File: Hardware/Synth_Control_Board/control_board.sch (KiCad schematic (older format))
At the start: 90 parts, among them J1 Conn_02x13_Odd_Even, J10 Conn_01x05, J11 Conn_01x08, J2 Conn_01x03, J3 Conn_02x13_Odd_Even, J4 Conn_01x08, J7 Conn_01x05, J8 Conn_01x05, J9 Conn_01x05, SW1 SW_DPDT_x2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

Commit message: fix net naming error on control board
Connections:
- net delay_in_1 is gone; now on net delay_fb_in: RV26.1
- net delay_in_2 is gone; now on net delay_time_in: RV27.1
- net delay_out_1 is gone; now on net delay_fb_out: RV26.2
- net delay_out_2 is gone; now on net delay_time_out: RV27.2
- net delay_out_3 is gone; now on net delay_mix_out: RV28.3
- net delay_in: no longer J4.5 (Pin_5)
- net delay_in_3 renamed delay_mix_in
- net delay_mix_in: now also J4.5 (Pin_5)
- net delay_out renamed delay_mix_out
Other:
- note added: "Global FB knob"
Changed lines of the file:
@@
 Delay controls
 Text Label 5600 4650 0    60   ~ 0
-delay_in_1
+delay_fb_in
 Text Label 5600 4750 0    60   ~ 0
-delay_out_1
+delay_fb_out
 Text Label 5600 4850 0    60   ~ 0
-delay_in_2
+delay_time_in
 Text Label 5600 4950 0    60   ~ 0
-delay_out_2
+delay_time_out
 Text Label 5600 5050 0    60   ~ 0
-delay_in_3
+delay_mix_in
 Text Label 5600 5150 0    60   ~ 0
-delay_out_3
+delay_mix_out
 Text Label 5350 6950 2    60   ~ 0
 delay_fb_in
@@
 delay_time_out
 Text Label 5350 7350 2    60   ~ 0
-delay_in
+delay_mix_in
 Text Label 5350 7450 2    60   ~ 0
-delay_out
+delay_mix_out
 $Comp
 L Conn_02x13_Odd_Even J1
@@
 	1    0    0    -1
 $EndComp
+Text Notes 3650 7900 0    60   ~ 0
+Global FB knob
 $EndSCHEMATC

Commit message: fix backward filter potentiometers
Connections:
- net freq_fb_1: now also RV17.A2 (S); no longer RV17.B2 (S)
- net freq_fb_2: now also RV14.A2 (S); no longer RV14.B2 (S)
- net freq_fb_3: now also RV15.A2 (S); no longer RV15.B2 (S)
- net freq_fb_4: now also RV16.A2 (S); no longer RV16.B2 (S)
- net freq_in_1: no longer RV17.A2 (S)
- net freq_in_2: no longer RV14.A2 (S)
- net freq_in_3: no longer RV15.A2 (S)
- net freq_in_4: no longer RV16.A2 (S)
- net freq_out_1: now also RV17.B2 (S)
- net freq_out_2: now also RV14.B2 (S)
- net freq_out_3: now also RV15.B2 (S)
- net freq_out_4: now also RV16.B2 (S)
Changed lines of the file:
@@
 Text Label 1800 6000 2    60   ~ 0
 freq_fb_1
-Text Label 1800 6600 2    60   ~ 0
+Text Label 1800 6550 2    60   ~ 0
 freq_fb_2
 Text Label 1800 7050 2    60   ~ 0
@@
 	1800 6300 2000 6300
 Wire Wire Line
-	1950 6050 2300 6050
-Connection ~ 1150 6300
-Wire Wire Line
 	1000 6300 1200 6300
 Wire Wire Line
-	1150 6050 1150 6300
-Wire Wire Line
-	1150 6050 1500 6050
-Wire Wire Line
 	8900 1700 9150 1700
 Wire Wire Line
@@
 	1400 6650 1400 6600
 Wire Wire Line
-	1400 6600 1050 6600
-Wire Wire Line
-	1050 6600 1050 6850
-Connection ~ 1050 6850
-Wire Wire Line
-	1800 6600 1800 6850
+	1800 6550 1800 6850
 Connection ~ 1800 6850
 Wire Wire Line
 	2250 6650 2250 6600
 Wire Wire Line
-	2250 6600 1900 6600
-Wire Wire Line
-	1900 6600 1900 6850
-Connection ~ 1900 6850
-Wire Wire Line
 	950  7350 1100 7350
 Wire Wire Line
 	1400 7150 1400 7100
-Wire Wire Line
-	1400 7100 1050 7100
-Wire Wire Line
-	1050 7100 1050 7350
-Connection ~ 1050 7350
 Wire Wire Line
 	1700 7350 1950 7350
@@
 	2250 7150 2250 7100
 Wire Wire Line
-	2250 7100 1900 7100
-Wire Wire Line
-	1900 7100 1900 7350
-Connection ~ 1900 7350
-Wire Wire Line
 	2550 7350 2750 7350
 Wire Wire Line
@@
 Wire Wire Line
 	1400 7600 1400 7550
-Wire Wire Line
-	1400 7550 1050 7550
-Wire Wire Line
-	1050 7550 1050 7800
-Connection ~ 1050 7800
 Wire Wire Line
 	1700 7800 1950 7800
@@
 	2250 7600 2250 7550
 Wire Wire Line
-	2250 7550 1900 7550
-Wire Wire Line
-	1900 7550 1900 7800
-Connection ~ 1900 7800
-Wire Wire Line
 	2550 7800 2750 7800
-Wire Wire Line
-	1950 6050 1950 6300
-Connection ~ 1950 6300
 $Comp
 L POT_DUAL RV17
@@
 Text Notes 3650 7900 0    60   ~ 0
 Global FB knob
+Wire Wire Line
+	1500 6050 1800 6050
+Connection ~ 1800 6050
+Wire Wire Line
+	2300 6050 2650 6050
+Wire Wire Line
+	2650 6050 2650 6300
+Connection ~ 2650 6300
+Wire Wire Line
+	2250 6600 2650 6600
+Wire Wire Line
+	2650 6600 2650 6850
+Connection ~ 2650 6850
+Wire Wire Line
+	2250 7100 2650 7100
+Wire Wire Line
+	2650 7100 2650 7350
+Connection ~ 2650 7350
+Wire Wire Line
+	2250 7550 2650 7550
+Wire Wire Line
+	2650 7550 2650 7800
+Connection ~ 2650 7800
+Wire Wire Line
+	1400 7550 1800 7550
+Connection ~ 1800 7550
+Wire Wire Line
+	1400 7100 1800 7100
+Connection ~ 1800 7100
+Wire Wire Line
+	1400 6600 1800 6600
+Connection ~ 1800 6600
 $EndSCHEMATC

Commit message: increase delay time pot value. End stop resistor is still fine.
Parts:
- RV27: value 20kA -> 100kA
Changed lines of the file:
@@
 P 4650 4700
 F 0 "RV27" V 4475 4700 50  0000 C CNN
-F 1 "20kA" V 4550 4700 50  0000 C CNN
+F 1 "100kA" V 4550 4700 50  0000 C CNN
 F 2 "Potentiometers:Potentiometer_Bourns_PTV09A-1_Horizontal" H 4650 4700 50  0001 C CNN
 F 3 "" H 4650 4700 50  0001 C CNN

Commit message: change delay fb control to log taper.
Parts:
- RV26: value 50kA -> 50kB
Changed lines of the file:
@@
 P 4650 4050
 F 0 "RV26" V 4475 4050 50  0000 C CNN
-F 1 "50kA" V 4550 4050 50  0000 C CNN
+F 1 "50kB" V 4550 4050 50  0000 C CNN
 F 2 "Potentiometers:Potentiometer_Bourns_PTV09A-1_Horizontal" H 4650 4050 50  0001 C CNN
 F 3 "" H 4650 4050 50  0001 C CNN

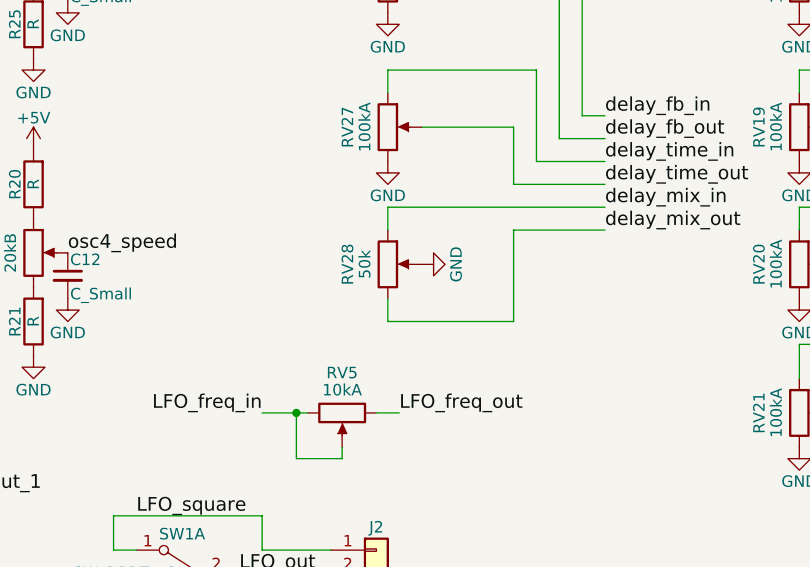
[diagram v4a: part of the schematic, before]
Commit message: WIP, delay mix control -> dual pot
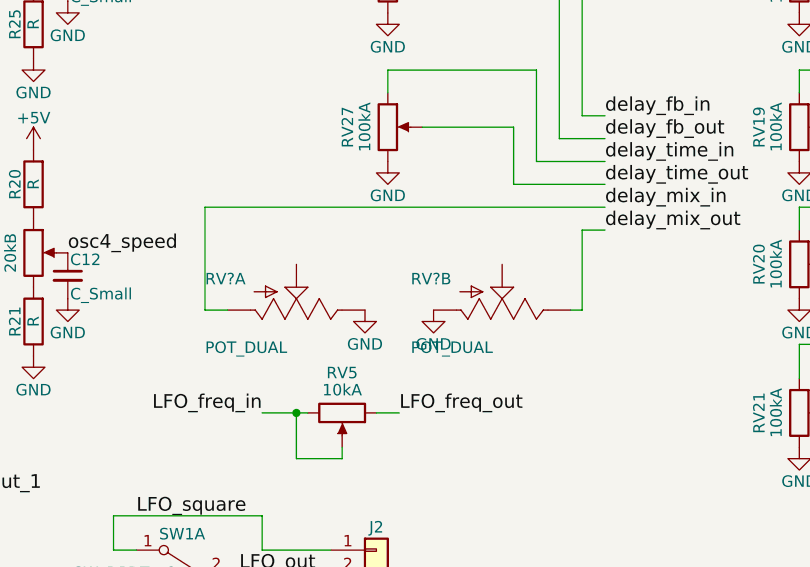
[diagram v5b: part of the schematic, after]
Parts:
- removed RV28: 50k, Potentiometers:Potentiometer_Bourns_PTV09A-1_Horizontal, symbol POT
- added RV? (x2): POT_DUAL, SparkFun-Electromechanical:POT_PANASONIC_DUAL_VERT_KIT, symbol POT_DUAL
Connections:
- net GND: now also RV?.A1 (E), RV?.B3 (A)
- net delay_mix_in: now also RV?.A3 (A)
- net delay_mix_out: now also RV?.B1 (E)
